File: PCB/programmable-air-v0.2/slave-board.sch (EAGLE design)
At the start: 37 parts, among them IC1 INA126U, IC3 LM358MX, Q1 600mA/40V, Q2 600mA/40V, Q3 600mA/40V

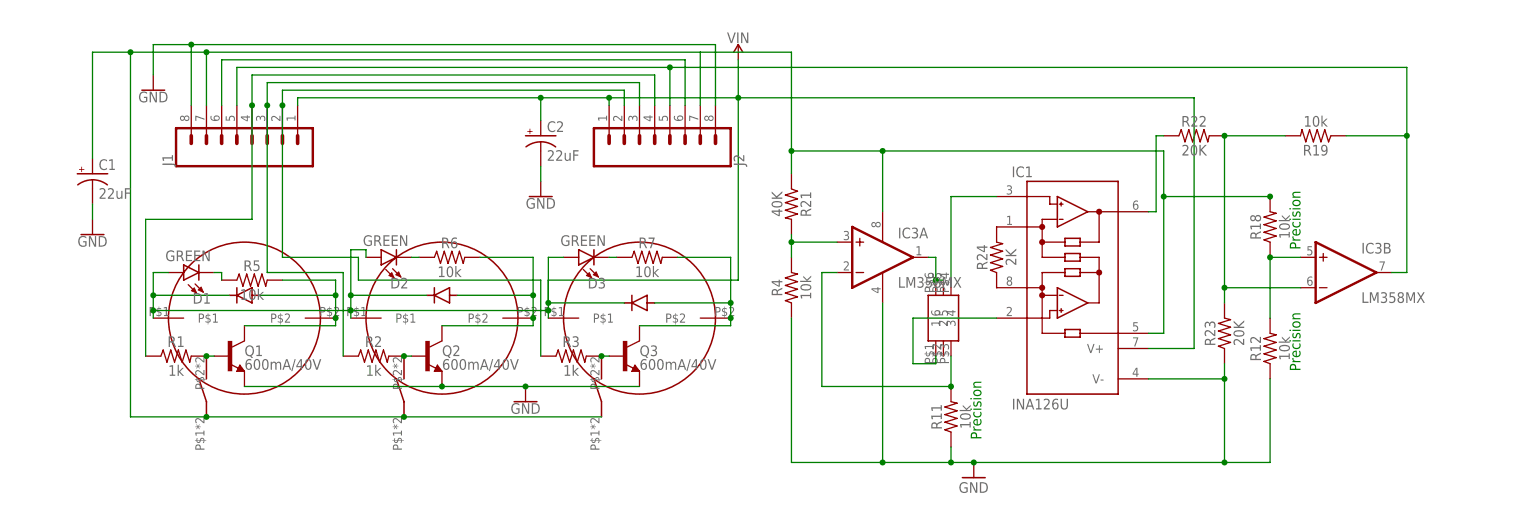
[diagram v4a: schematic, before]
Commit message: Master board + Slave board in single PCB ready.
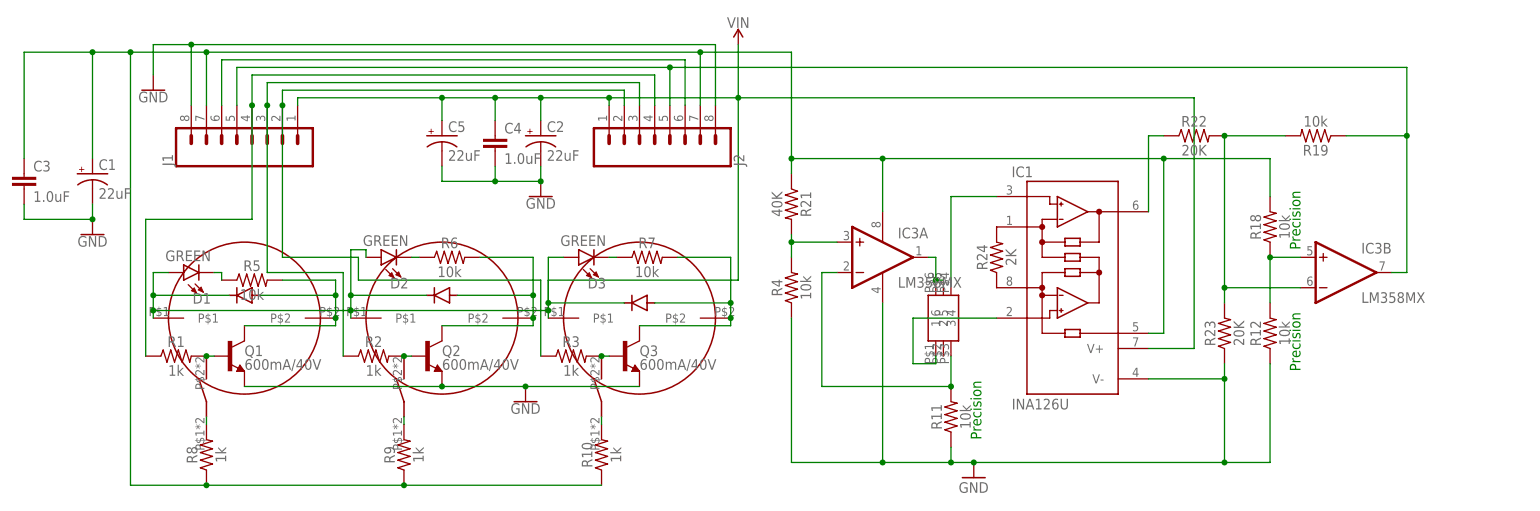
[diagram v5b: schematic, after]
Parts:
- added C3, C4: 1.0uF, SparkFun-Capacitors:1.0UF-0603-16V-10%
- added C5: 22uF, SparkFun-Capacitors:22UF-POLAR-PANASONIC_C-35V-20%
- added R10, R8, R9: 1k, SparkFun-Resistors:1KOHM-0603-1/10W-1%
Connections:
- removed net N$15: C1.+, IC1.REF, IC3P.V+, J1.7, J2.7, R18.2, R21.1, U$10.P$1, U$8.P$1, U$9.P$1
- removed net VIN: C2.+, D1.A, D2.A, D3.A, IC1.V+, J1.1, J2.1, U$2.P$1, U$3.P$1, U$4.P$1, U$5.P$1, U$6.P$1, U$7.P$1
- new net N$17: C2.+, C4.1, C5.+, D1.A, D2.A, D3.A, IC1.V+, J1.1, J2.1, U$2.P$1, U$3.P$1, U$4.P$1, U$5.P$1, U$6.P$1, U$7.P$1
- new net N$21: R8.2, U$8.P$1
- new net N$22: R9.2, U$9.P$1
- new net N$23: R10.2, U$10.P$1
- new net N$28: C1.+, C3.1, IC1.REF, IC3P.V+, J1.7, J2.7, R10.1, R18.2, R21.1, R8.1, R9.1
- net GND: now also C3.2, C4.2, C5.-
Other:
- moved on the sheet: R12
